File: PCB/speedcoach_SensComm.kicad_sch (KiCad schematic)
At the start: 14 parts, among them J1 Conn_01x04_Male, J2 Conn_01x04_Male, U1 PA1010D, U2 DA14531MOD, U3 ORG1411-PM04, U4 GLCD_2.7INCH, U5 PIM456

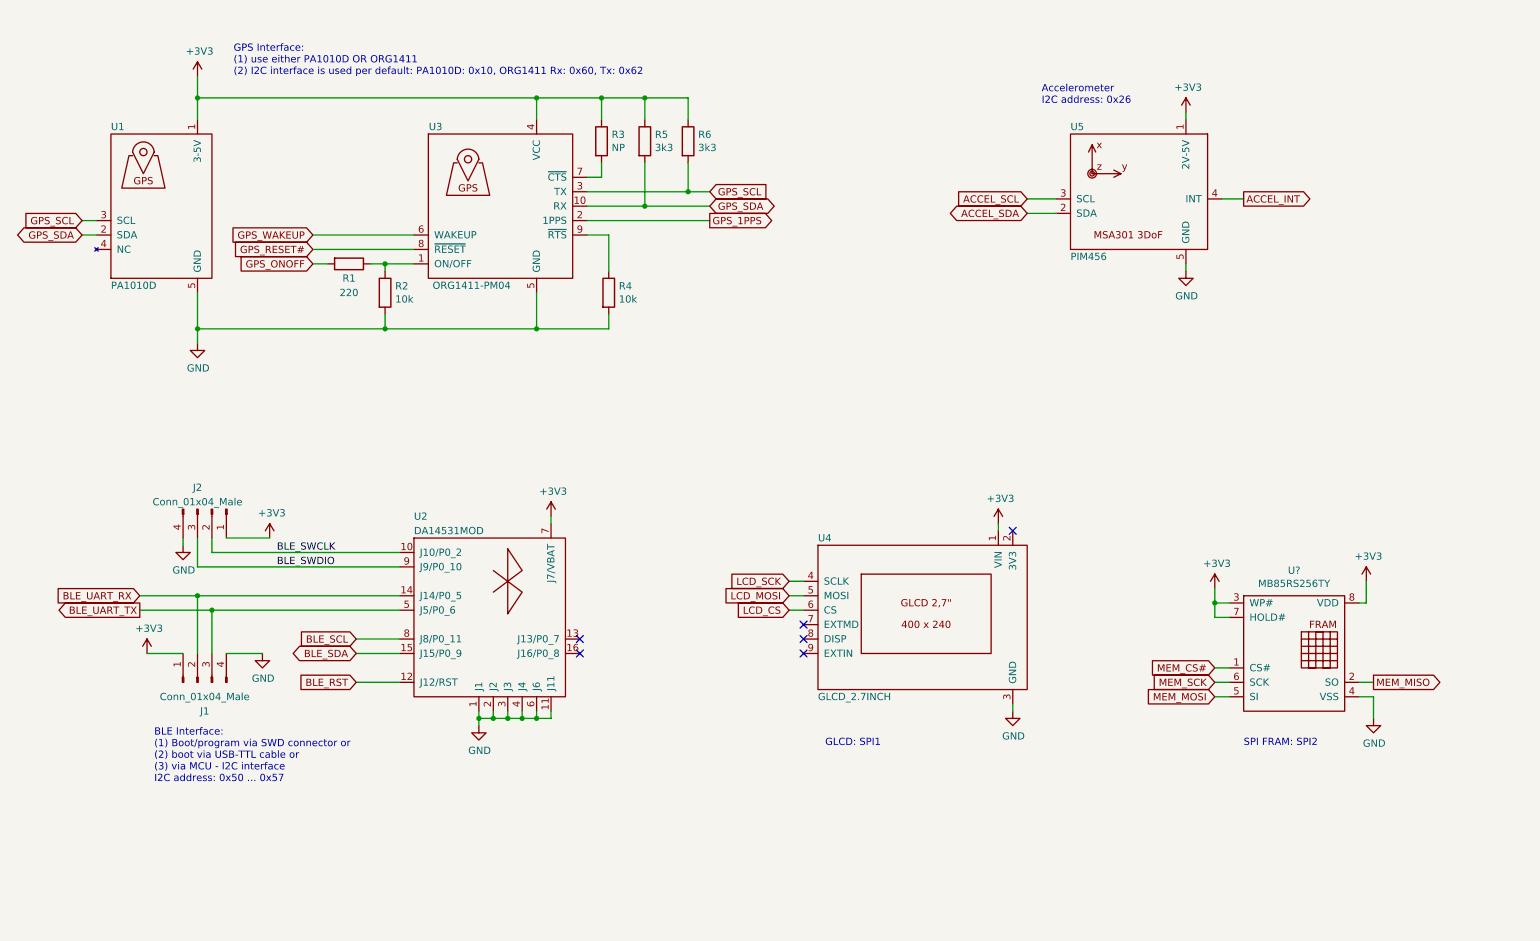
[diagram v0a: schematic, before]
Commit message: added Bluefruit module
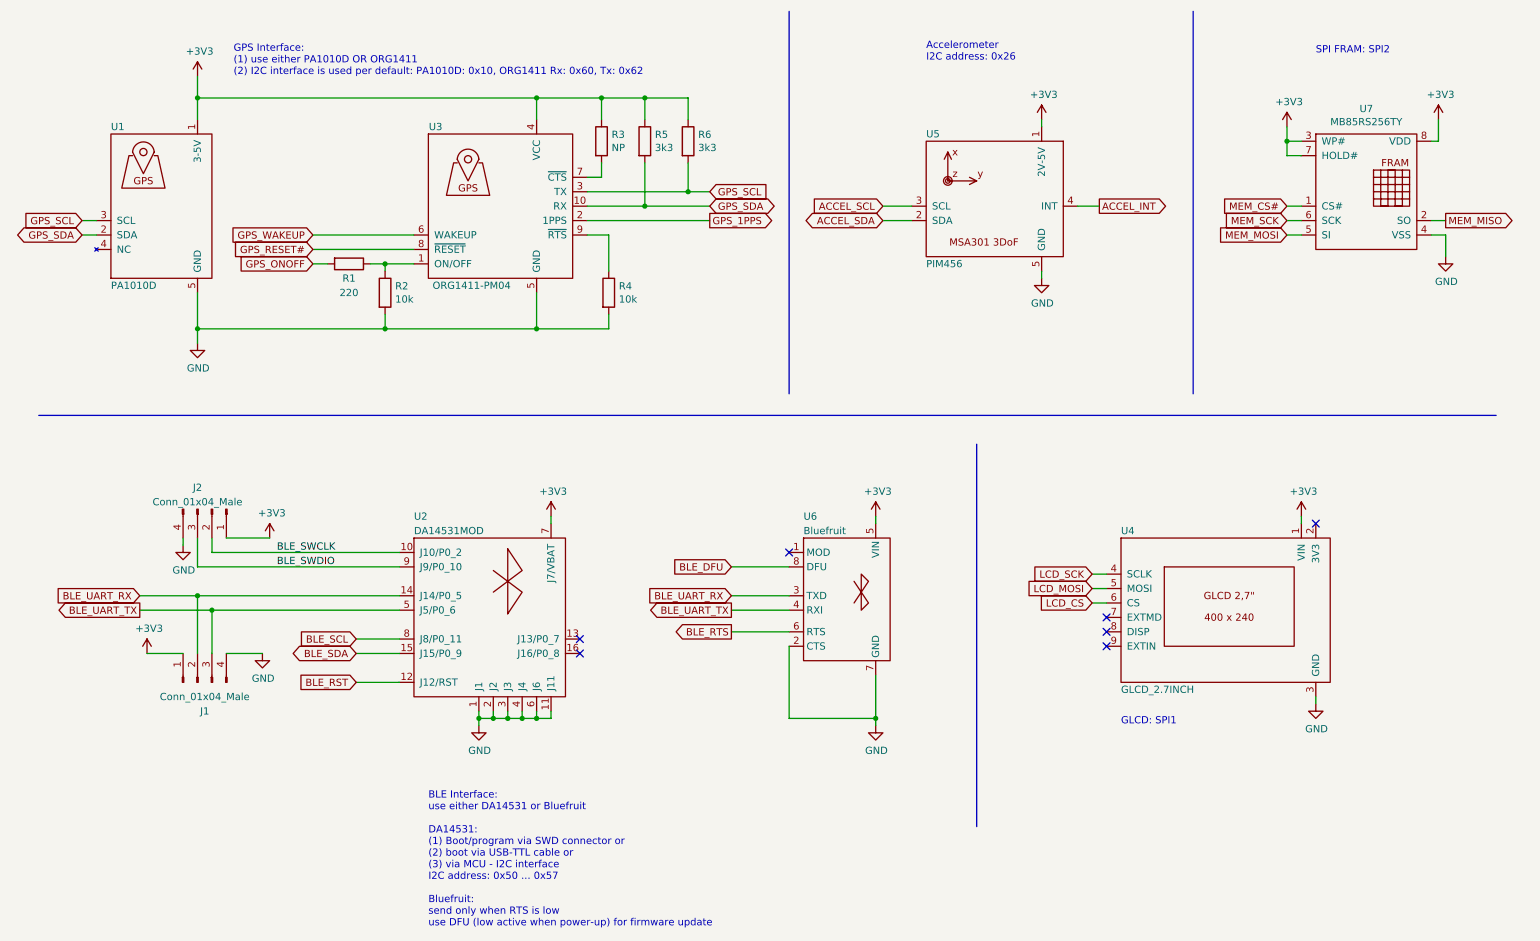
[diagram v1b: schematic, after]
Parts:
- added U6: Bluefruit, symbol speedcoach:Bluefruit
- gave numbers to parts that had none: 1
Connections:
- net +3V3: now also U6.5 (VIN)
- net BLE_UART_RX: now also U6.3 (TXD)
- net BLE_UART_TX: now also U6.4 (RXI)
- net GND: now also U6.2 (CTS), U6.7 (GND)
- new net BLE_DFU: U6.8 (DFU)
- new net BLE_RTS: U6.6 (RTS)
- no-connect marks 6 -> 7
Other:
- note added: "BLE Interface: use either DA14531 or Bluefruit DA14531: (1) Boot/program via SWD connector or (2) boot via USB-TTL cable or (3) via MCU - I2C interface I2C address: 0x50 ... 0x57 Bluefruit: send only when RTS is low use DFU (low active when power-up) for firmware update"
- note removed: "BLE Interface: (1) Boot/program via SWD connector or (2) boot via USB-TTL cable or (3) via MCU - I2C interface I2C address: 0x50 ... 0x57"
- moved on the sheet: U4, U5, U7

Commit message: revised MCU
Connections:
- net BLE_SCL is gone; now on net BLE_ACCEL_SCL: U2.8 (J8/P0_11)
- net BLE_SDA is gone; now on net BLE_ACCEL_SDA: U2.15 (J15/P0_9)
- net ACCEL_SCL renamed BLE_ACCEL_SCL
- net ACCEL_SDA renamed BLE_ACCEL_SDA

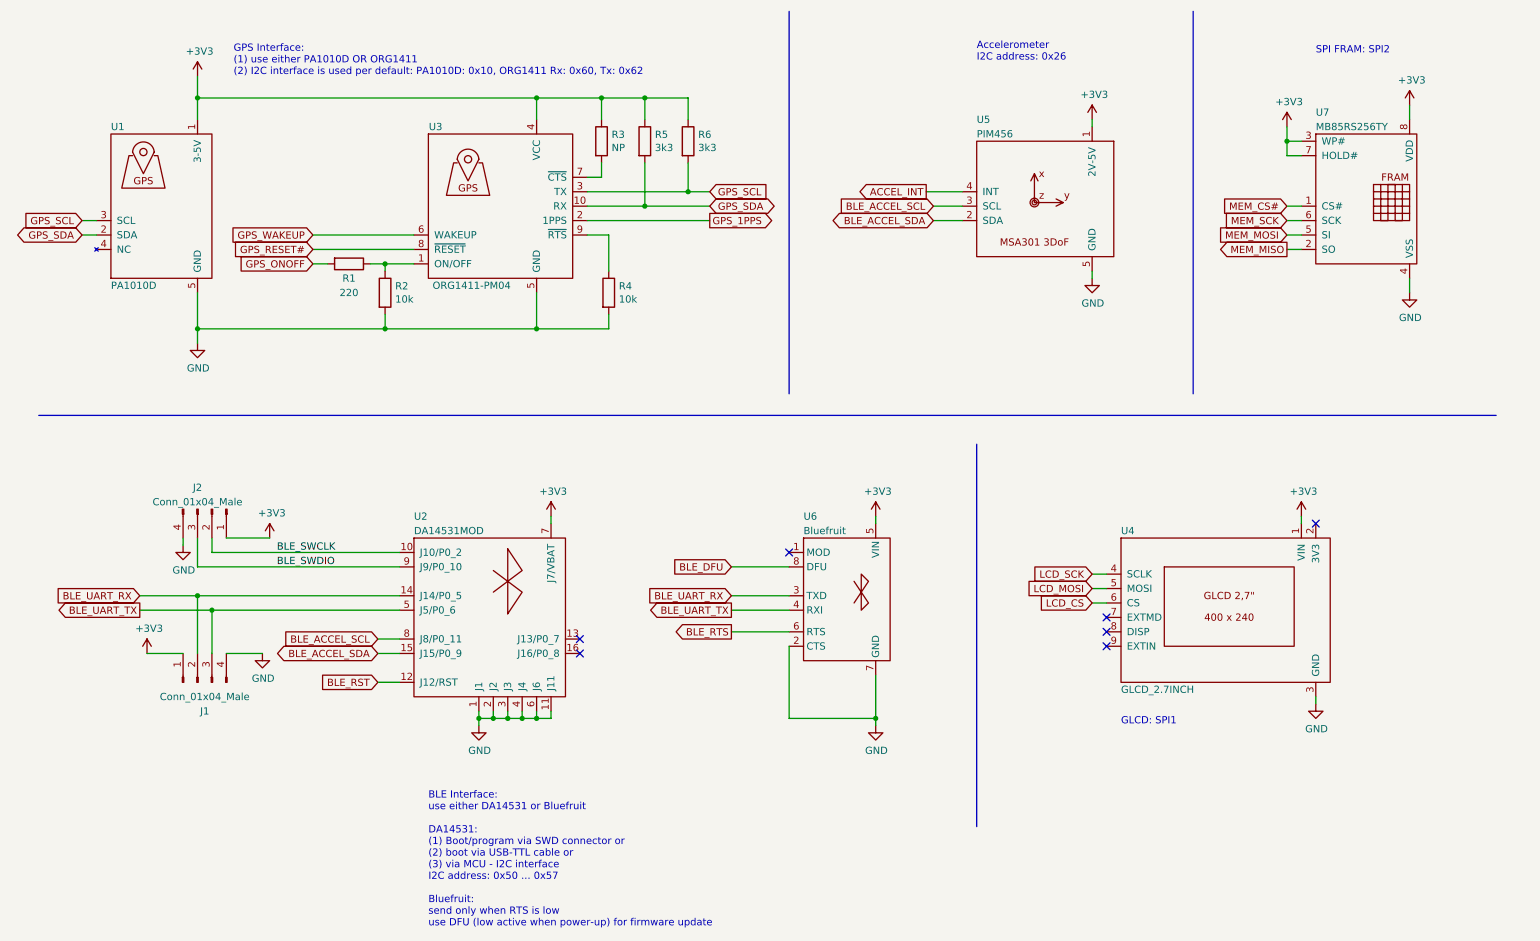
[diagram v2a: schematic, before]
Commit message: updated some labels, finetuning
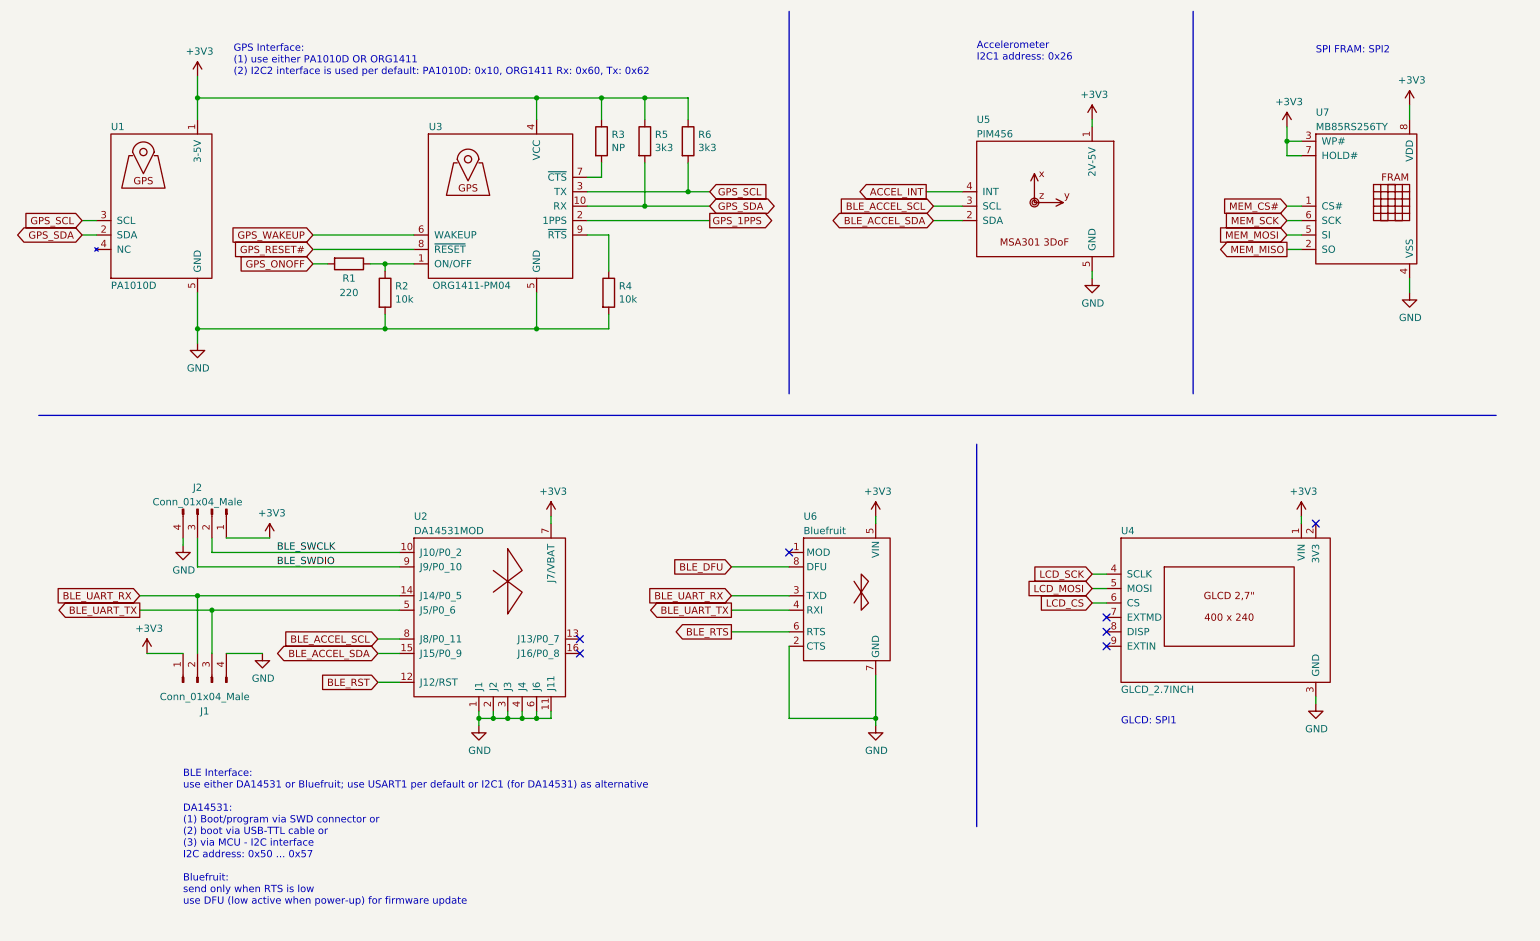
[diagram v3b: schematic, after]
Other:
- note added: "Accelerometer I2C1 address: 0x26"
- note added: "BLE Interface: use either DA14531 or Bluefruit; use USART1 per default or I2C1 (for DA14531) as alternative DA14531: (1) Boot/program via SWD connector or (2) boot via USB-TTL cable or (3) via MCU - I2C interface I2C address: 0x50 ... 0x57 Bluefruit: send only when RTS is low use DFU (low active when power-up) for firmware update"
- note added: "GPS Interface: (1) use either PA1010D OR ORG1411 (2) I2C2 interface is used per default: PA1010D: 0x10, ORG1411 Rx: 0x60, Tx: 0x62"
- note removed: "Accelerometer I2C address: 0x26"
- note removed: "BLE Interface: use either DA14531 or Bluefruit DA14531: (1) Boot/program via SWD connector or (2) boot via USB-TTL cable or (3) via MCU - I2C interface I2C address: 0x50 ... 0x57 Bluefruit: send only when RTS is low use DFU (low active when power-up) for firmware update"
- note removed: "GPS Interface: (1) use either PA1010D OR ORG1411 (2) I2C interface is used per default: PA1010D: 0x10, ORG1411 Rx: 0x60, Tx: 0x62"
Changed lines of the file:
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@@
     (stroke (width 0) (type default))
   )
-  (text "Accelerometer\nI2C address: 0x26" (at 186.69 26.67 0)
+  (text "Accelerometer\nI2C1 address: 0x26" (at 186.69 26.67 0)
     (effects (font (size 1.27 1.27)) (justify left bottom))
   )
@@
     (effects (font (size 1.27 1.27)) (justify left bottom))
   )
-  (text "GPS Interface:\n(1) use either PA1010D OR ORG1411\n(2) I2C interface is used per default: PA1010D: 0x10, ORG1411 Rx: 0x60, Tx: 0x62"
+  (text "GPS Interface:\n(1) use either PA1010D OR ORG1411\n(2) I2C2 interface is used per default: PA1010D: 0x10, ORG1411 Rx: 0x60, Tx: 0x62"
     (at 55.88 29.21 0)
     (effects (font (size 1.27 1.27)) (justify left bottom))
   )
-  (text "BLE Interface:\nuse either DA14531 or Bluefruit\n\nDA14531:\n(1) Boot/program via SWD connector or\n(2) boot via USB-TTL cable or\n(3) via MCU - I2C interface\nI2C address: 0x50 ... 0x57\n\nBluefruit:\nsend only when RTS is low\nuse DFU (low active when power-up) for firmware update"
-    (at 90.17 179.07 0)
+  (text "BLE Interface:\nuse either DA14531 or Bluefruit; use USART1 per default or I2C1 (for DA14531) as alternative\n\nDA14531:\n(1) Boot/program via SWD connector or\n(2) boot via USB-TTL cable or\n(3) via MCU - I2C interface\nI2C address: 0x50 ... 0x57\n\nBluefruit:\nsend only when RTS is low\nuse DFU (low active when power-up) for firmware update"
+    (at 46.99 175.26 0)
     (effects (font (size 1.27 1.27)) (justify left bottom))
   )
@@
   (global_label "MEM_SCK" (shape input) (at 241.3 54.61 180) (fields_autoplaced)
     (effects (font (size 1.27 1.27)) (justify right))
-    (property "Intersheetrefs" "${INTERSHEET_REFS}" (id 0) (at 230.6616 54.61 0)
-      (effects (font (size 1.27 1.27)) (justify right))
+    (property "Intersheetrefs" "${INTERSHEET_REFS}" (id 0) (at 230.4383 54.61 0)
+      (effects (font (size 1.27 1.27)) (justify right) hide)
     )
   )
   (global_label "MEM_MOSI" (shape input) (at 241.3 57.15 180) (fields_autoplaced)
     (effects (font (size 1.27 1.27)) (justify right))
-    (property "Intersheetrefs" "${INTERSHEET_REFS}" (id 0) (at 229.9873 57.15 0)
-      (effects (font (size 1.27 1.27)) (justify right))
+    (property "Intersheetrefs" "${INTERSHEET_REFS}" (id 0) (at 229.5916 57.15 0)
+      (effects (font (size 1.27 1.27)) (justify right) hide)
     )
   )
@@
   (global_label "MEM_CS#" (shape input) (at 241.3 52.07 180) (fields_autoplaced)
     (effects (font (size 1.27 1.27)) (justify right))
-    (property "Intersheetrefs" "${INTERSHEET_REFS}" (id 0) (at 230.5406 52.07 0)
-      (effects (font (size 1.27 1.27)) (justify right))
+    (property "Intersheetrefs" "${INTERSHEET_REFS}" (id 0) (at 230.4383 52.07 0)
+      (effects (font (size 1.27 1.27)) (justify right) hide)
     )
   )
@@
     (effects (font (size 1.27 1.27)) (justify right))
     (property "Intersheetrefs" "${INTERSHEET_REFS}" (id 0) (at 133.3134 115.57 0)
-      (effects (font (size 1.27 1.27)) (justify right))
+      (effects (font (size 1.27 1.27)) (justify right) hide)
     )
   )
@@
     (effects (font (size 1.27 1.27)) (justify right))
     (property "Intersheetrefs" "${INTERSHEET_REFS}" (id 0) (at 133.5554 127 0)
-      (effects (font (size 1.27 1.27)) (justify right))
+      (effects (font (size 1.27 1.27)) (justify right) hide)
     )
   )
@@
     (effects (font (size 1.27 1.27)) (justify right))
     (property "Intersheetrefs" "${INTERSHEET_REFS}" (id 0) (at 229.5916 59.69 0)
-      (effects (font (size 1.27 1.27)) (justify right))
+      (effects (font (size 1.27 1.27)) (justify right) hide)
     )
   )

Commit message: placement
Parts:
- added C10: 100nF, Capacitor_SMD:C_0805_2012Metric, symbol Device:C
- R1, R2, R3, R4, R5, R6: footprint (none) -> Resistor_SMD:R_0805_2012Metric
- U6: footprint (none) -> speedcoach:Bluefruit
- U7: footprint (none) -> Package_SO:SOP-8_3.9x4.9mm_P1.27mm
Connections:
- net +3V3: now also C10.1
- net GND: now also C10.2
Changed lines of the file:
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@@
   (junction (at 104.14 142.24) (diameter 0) (color 0 0 0 0)
   )
+  (junction (at 262.89 66.04) (diameter 0) (color 0 0 0 0)
+  )
   (junction (at 109.22 142.24) (diameter 0) (color 0 0 0 0)
   )
@@
   )
   (junction (at 128.27 52.07) (diameter 0) (color 0 0 0 0)
+  )
+  (junction (at 262.89 35.56) (diameter 0) (color 0 0 0 0)
   )
   (junction (at 82.55 62.23) (diameter 0) (color 0 0 0 0)
@@
     (stroke (width 0) (type default))
   )
+  (wire (pts (xy 271.78 35.56) (xy 271.78 46.99))
+    (stroke (width 0) (type default))
+  )
   (wire (pts (xy 143.51 115.57) (xy 153.67 115.57))
     (stroke (width 0) (type default))
@@
     (stroke (width 0) (type default))
   )
-  (wire (pts (xy 262.89 64.77) (xy 262.89 67.31))
+  (wire (pts (xy 262.89 64.77) (xy 262.89 66.04))
+    (stroke (width 0) (type default))
+  )
+  (wire (pts (xy 271.78 66.04) (xy 262.89 66.04))
     (stroke (width 0) (type default))
   )
@@
     (stroke (width 0) (type default))
   )
-  (wire (pts (xy 262.89 34.29) (xy 262.89 36.83))
+  (wire (pts (xy 262.89 34.29) (xy 262.89 35.56))
     (stroke (width 0) (type default))
   )
@@
     (stroke (width 0) (type default))
   )
+  (wire (pts (xy 271.78 54.61) (xy 271.78 66.04))
+    (stroke (width 0) (type default))
+  )
   (wire (pts (xy 52.07 110.49) (xy 52.07 113.03))
     (stroke (width 0) (type default))
@@
     (stroke (width 0) (type default))
   )
+  (wire (pts (xy 262.89 35.56) (xy 271.78 35.56))
+    (stroke (width 0) (type default))
+  )
+  (wire (pts (xy 262.89 35.56) (xy 262.89 36.83))
+    (stroke (width 0) (type default))
+  )
   (wire (pts (xy 72.39 62.23) (xy 69.85 62.23))
     (stroke (width 0) (type default))
@@
   )
   (wire (pts (xy 81.28 135.89) (xy 85.09 135.89))
+    (stroke (width 0) (type default))
+  )
+  (wire (pts (xy 262.89 66.04) (xy 262.89 67.31))
     (stroke (width 0) (type default))
   )
@@
       (effects (font (size 1.27 1.27)))
     )
-    (property "Footprint" "" (id 2) (at 76.2 60.452 90)
+    (property "Footprint" "Resistor_SMD:R_0805_2012Metric" (id 2) (at 76.2 60.452 90)
       (effects (font (size 1.27 1.27)) hide)
     )
@@
       (effects (font (size 1.27 1.27)) (justify left))
     )
-    (property "Footprint" "" (id 2) (at 80.772 67.31 90)
+    (property "Footprint" "Resistor_SMD:R_0805_2012Metric" (id 2) (at 80.772 67.31 90)
       (effects (font (size 1.27 1.27)) hide)
     )
@@
       (effects (font (size 1.27 1.27)) (justify left))
     )
-    (property "Footprint" "" (id 2) (at 134.112 40.64 90)
+    (property "Footprint" "Resistor_SMD:R_0805_2012Metric" (id 2) (at 134.112 40.64 90)
       (effects (font (size 1.27 1.27)) hide)
     )
@@
       (effects (font (size 1.27 1.27)) (justify left))
     )
-    (property "Footprint" "" (id 2) (at 126.492 40.64 90)
+    (property "Footprint" "Resistor_SMD:R_0805_2012Metric" (id 2) (at 126.492 40.64 90)
       (effects (font (size 1.27 1.27)) hide)
     )
@@
       (effects (font (size 1.27 1.27)) (justify left))
     )
-    (property "Footprint" "" (id 2) (at 120.142 67.31 90)
+    (property "Footprint" "Resistor_SMD:R_0805_2012Metric" (id 2) (at 120.142 67.31 90)
       (effects (font (size 1.27 1.27)) hide)
     )
@@
       (effects (font (size 1.27 1.27)) (justify left))
     )
-    (property "Footprint" "" (id 2) (at 118.872 40.64 90)
+    (property "Footprint" "Resistor_SMD:R_0805_2012Metric" (id 2) (at 118.872 40.64 90)
       (effects (font (size 1.27 1.27)) hide)
     )
@@
       (effects (font (size 1.27 1.27)) (justify left))
     )
-    (property "Footprint" "" (id 2) (at 246.38 59.69 0)
+    (property "Footprint" "Package_SO:SOP-8_3.9x4.9mm_P1.27mm" (id 2) (at 246.38 59.69 0)
       (effects (font (size 1.27 1.27)) hide)
     )
@@
       (effects (font (size 1.27 1.27)) (justify left))
     )
-    (property "Footprint" "" (id 2) (at 153.67 129.54 0)
+    (property "Footprint" "speedcoach:Bluefruit" (id 2) (at 153.67 129.54 0)
       (effects (font (size 1.27 1.27)) hide)
     )
@@
     (pin "8")
   )
+  (symbol (lib_id "Device:C") (at 271.78 50.8 0) (mirror y) (unit 1)
+    (in_bom yes) (on_board yes)
+    (property "Reference" "C10" (id 0) (at 274.6756 51.9684 0)
+      (effects (font (size 1.27 1.27)) (justify right))
+    )
+    (property "Value" "100nF" (id 1) (at 274.6756 49.657 0)
+      (effects (font (size 1.27 1.27)) (justify right))
+    )
+    (property "Footprint" "Capacitor_SMD:C_0805_2012Metric" (id 2) (at 270.8148 54.61 0)
+      (effects (font (size 1.27 1.27)) hide)
+    )
+    (property "Datasheet" "~" (id 3) (at 271.78 50.8 0)
+      (effects (font (size 1.27 1.27)) hide)
+    )
+    (pin "1")
+    (pin "2")
+  )
 )

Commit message: routed v1
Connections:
- net BLE_SWCLK: now also J2.3 (Pin_3); no longer J2.2 (Pin_2)
- net BLE_SWDIO: now also J2.2 (Pin_2); no longer J2.3 (Pin_3)
- net BLE_UART_RX: now also J1.3 (Pin_3); no longer J1.2 (Pin_2)
- net BLE_UART_TX: now also J1.2 (Pin_2); no longer J1.3 (Pin_3)
